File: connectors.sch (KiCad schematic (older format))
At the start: 4 parts

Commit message: finished schematic for review
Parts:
- removed J? (x3): Conn_01x06, symbol Connector_Generic:Conn_01x06
- added J? (x3): Conn_01x07, symbol Connector_Generic:Conn_01x07
- added J?: XLR5, symbol Connector:XLR5
- added R? (x15): 1K, symbol Device:R
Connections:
- net +12V: now also J?.1 (Pin_1), J?.1 (Pin_1), J?.1 (Pin_1)
- net Ch_1: now also J?.2 (Pin_2), R?.1
- net Ch_10: now also J?.6 (Pin_6), R?.1
- net Ch_11: now also J?.2 (Pin_2), R?.1
- net Ch_12: now also J?.3 (Pin_3), R?.1
- net Ch_2: now also J?.3 (Pin_3), R?.1
- net Ch_3: now also J?.4 (Pin_4), R?.1
- net Ch_4: now also J?.5 (Pin_5), R?.1
- net Ch_5: now also J?.6 (Pin_6), R?.1
- net Ch_6: now also J?.2 (Pin_2), R?.1
- net Ch_7: now also J?.3 (Pin_3), R?.1
- net Ch_8: now also J?.4 (Pin_4), R?.1
- net Ch_9: now also J?.5 (Pin_5), R?.1
- net GND: now also J?.4 (P3), J?.7 (Pin_7), J?.7 (Pin_7), J?.7 (Pin_7), R?.2, R?.2, R?.2, R?.2, R?.2, R?.2, R?.2, R?.2, R?.2, R?.2, R?.2, R?.2, R?.2, R?.2, R?.2
- net PPS: now also J?.3 (P3)
- net VCC: now also J?.5 (P5)
- net DI renamed RS485_A
- net RS485_A: now also J?.1 (P1)
- net RO renamed RS485_B
- net RS485_B: now also J?.2 (P2)
- new net Ch_13: J?.4 (Pin_4), R?.1
- new net Ch_14: J?.5 (Pin_5), R?.1
- new net Ch_15: J?.6 (Pin_6), R?.1

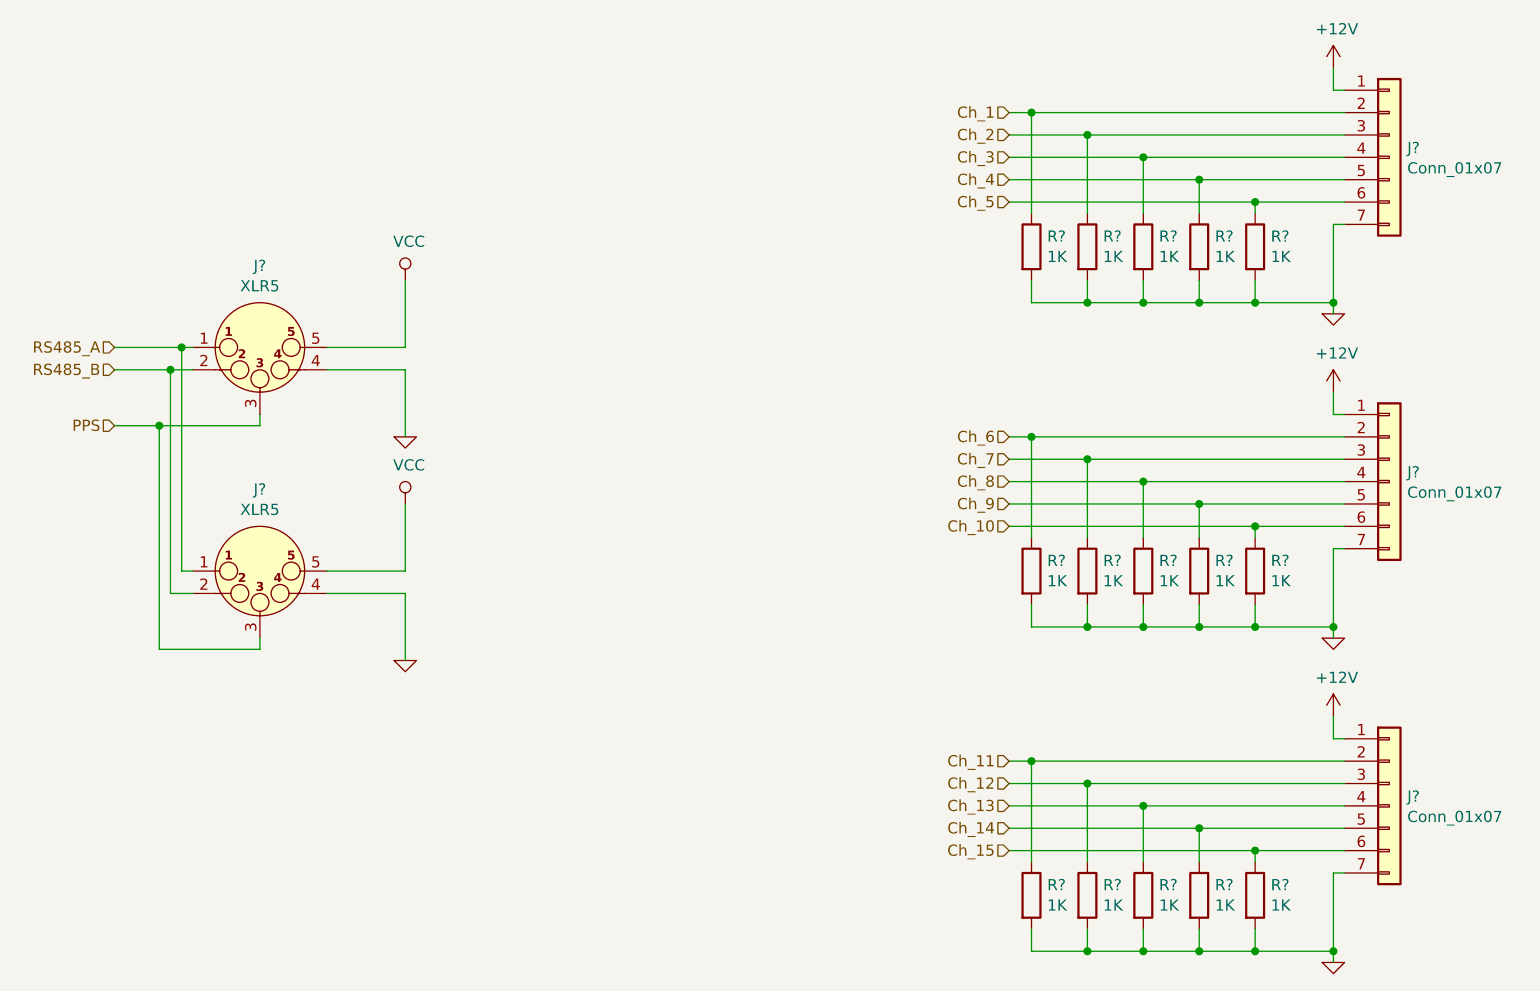
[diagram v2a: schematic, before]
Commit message: added pdf schematic
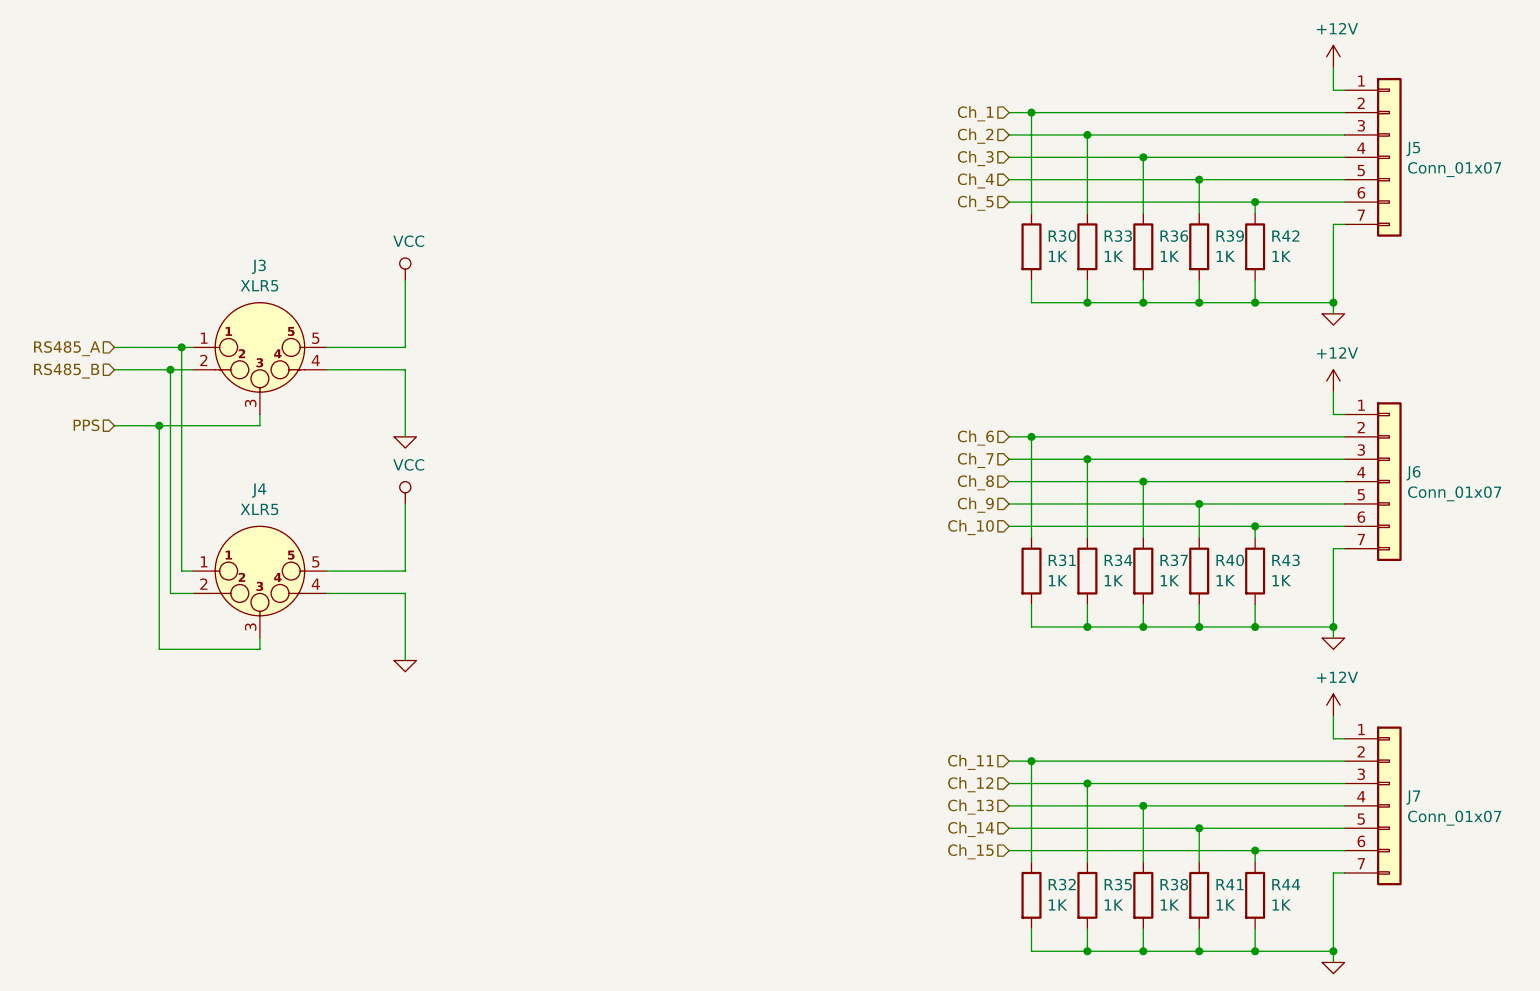
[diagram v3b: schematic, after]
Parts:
- gave numbers to parts that had none: 20
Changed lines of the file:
@@
 	8850 1750 8800 1750
 $Comp
-L daisy:GND #PWR?
+L daisy:GND #PWR052
 U 1 1 5D36F5B8
 P 8800 2150
-F 0 "#PWR?" H 8800 2150 30  0001 C CNN
+F 0 "#PWR052" H 8800 2150 30  0001 C CNN
 F 1 "GND" H 8800 2080 30  0001 C CNN
 F 2 "" H 8800 2150 60  0000 C CNN
@@
 	8800 1750 8800 2100
 $Comp
-L power:+12V #PWR?
+L power:+12V #PWR051
 U 1 1 5D36F5BF
 P 8800 1050
-F 0 "#PWR?" H 8800 900 50  0001 C CNN
+F 0 "#PWR051" H 8800 900 50  0001 C CNN
 F 1 "+12V" H 8815 1223 50  0000 C CNN
 F 2 "" H 8800 1050 50  0001 C CNN
@@
 Ch_4
 $Comp
-L Connector:XLR5 J?
+L Connector:XLR5 J3
 U 1 1 5D36FCC4
 P 4000 2300
-F 0 "J?" H 4000 2665 50  0000 C CNN
+F 0 "J3" H 4000 2665 50  0000 C CNN
 F 1 "XLR5" H 4000 2574 50  0000 C CNN
 F 2 "" H 4000 2300 50  0001 C CNN
@@
 	4300 2400 4650 2400
 $Comp
-L daisy:GND #PWR?
+L daisy:GND #PWR048
 U 1 1 5D37030E
 P 4650 2700
-F 0 "#PWR?" H 4650 2700 30  0001 C CNN
+F 0 "#PWR048" H 4650 2700 30  0001 C CNN
 F 1 "GND" H 4650 2630 30  0001 C CNN
 F 2 "" H 4650 2700 60  0000 C CNN
@@
 	4650 2400 4650 2700
 $Comp
-L power:VCC #PWR?
+L power:VCC #PWR047
 U 1 1 5D37054E
 P 4650 2000
-F 0 "#PWR?" H 4650 1850 50  0001 C CNN
+F 0 "#PWR047" H 4650 1850 50  0001 C CNN
 F 1 "VCC" H 4667 2173 50  0000 C CNN
 F 2 "" H 4650 2000 50  0001 C CNN
@@
 PPS
 $Comp
-L Connector_Generic:Conn_01x07 J?
+L Connector_Generic:Conn_01x07 J5
 U 1 1 5D5ED43F
 P 9050 1450
-F 0 "J?" H 9130 1492 50  0000 L CNN
+F 0 "J5" H 9130 1492 50  0000 L CNN
 F 1 "Conn_01x07" H 9130 1401 50  0000 L CNN
 F 2 "" H 9050 1450 50  0001 C CNN
@@
 Ch_5
 $Comp
-L Device:R R?
+L Device:R R42
 U 1 1 5D5EDE7E
 P 8450 1850
-F 0 "R?" H 8520 1896 50  0000 L CNN
+F 0 "R42" H 8520 1896 50  0000 L CNN
 F 1 "1K" H 8520 1805 50  0000 L CNN
 F 2 "" V 8380 1850 50  0001 C CNN
@@
 $EndComp
 $Comp
-L Device:R R?
+L Device:R R39
 U 1 1 5D5EE2E2
 P 8200 1850
-F 0 "R?" H 8270 1896 50  0000 L CNN
+F 0 "R39" H 8270 1896 50  0000 L CNN
 F 1 "1K" H 8270 1805 50  0000 L CNN
 F 2 "" V 8130 1850 50  0001 C CNN
@@
 $EndComp
 $Comp
-L Device:R R?
+L Device:R R36
 U 1 1 5D5EE304
 P 7950 1850
-F 0 "R?" H 8020 1896 50  0000 L CNN
+F 0 "R36" H 8020 1896 50  0000 L CNN
 F 1 "1K" H 8020 1805 50  0000 L CNN
 F 2 "" V 7880 1850 50  0001 C CNN
@@
 $EndComp
 $Comp
-L Device:R R?
+L Device:R R33
 U 1 1 5D5EE328
 P 7700 1850
-F 0 "R?" H 7770 1896 50  0000 L CNN
+F 0 "R33" H 7770 1896 50  0000 L CNN
 F 1 "1K" H 7770 1805 50  0000 L CNN
 F 2 "" V 7630 1850 50  0001 C CNN
@@
 $EndComp
 $Comp
-L Device:R R?
+L Device:R R30
 U 1 1 5D5EE34E
 P 7450 1850
-F 0 "R?" H 7520 1896 50  0000 L CNN
+F 0 "R30" H 7520 1896 50  0000 L CNN
 F 1 "1K" H 7520 1805 50  0000 L CNN
 F 2 "" V 7380 1850 50  0001 C CNN
@@
 	8850 3200 8800 3200
 $Comp
-L daisy:GND #PWR?
+L daisy:GND #PWR054
 U 1 1 5D5F47DC
 P 8800 3600
-F 0 "#PWR?" H 8800 3600 30  0001 C CNN
+F 0 "#PWR054" H 8800 3600 30  0001 C CNN
 F 1 "GND" H 8800 3530 30  0001 C CNN
 F 2 "" H 8800 3600 60  0000 C CNN
@@
 	8800 3200 8800 3550
 $Comp
-L power:+12V #PWR?
+L power:+12V #PWR053
 U 1 1 5D5F47E3
 P 8800 2500
-F 0 "#PWR?" H 8800 2350 50  0001 C CNN
+F 0 "#PWR053" H 8800 2350 50  0001 C CNN
 F 1 "+12V" H 8815 2673 50  0000 C CNN
 F 2 "" H 8800 2500 50  0001 C CNN
@@
 Ch_9
 $Comp
-L Connector_Generic:Conn_01x07 J?
+L Connector_Generic:Conn_01x07 J6
 U 1 1 5D5F47ED
 P 9050 2900
-F 0 "J?" H 9130 2942 50  0000 L CNN
+F 0 "J6" H 9130 2942 50  0000 L CNN
 F 1 "Conn_01x07" H 9130 2851 50  0000 L CNN
 F 2 "" H 9050 2900 50  0001 C CNN
@@
 Ch_10
 $Comp
-L Device:R R?
+L Device:R R43
 U 1 1 5D5F47F5
 P 8450 3300
-F 0 "R?" H 8520 3346 50  0000 L CNN
+F 0 "R43" H 8520 3346 50  0000 L CNN
 F 1 "1K" H 8520 3255 50  0000 L CNN
 F 2 "" V 8380 3300 50  0001 C CNN
@@
 $EndComp
 $Comp
-L Device:R R?
+L Device:R R40
 U 1 1 5D5F47FC
 P 8200 3300
-F 0 "R?" H 8270 3346 50  0000 L CNN
+F 0 "R40" H 8270 3346 50  0000 L CNN
 F 1 "1K" H 8270 3255 50  0000 L CNN
 F 2 "" V 8130 3300 50  0001 C CNN
@@
 $EndComp
 $Comp
-L Device:R R?
+L Device:R R37
 U 1 1 5D5F4803
 P 7950 3300
-F 0 "R?" H 8020 3346 50  0000 L CNN
+F 0 "R37" H 8020 3346 50  0000 L CNN
 F 1 "1K" H 8020 3255 50  0000 L CNN
 F 2 "" V 7880 3300 50  0001 C CNN
@@
 $EndComp
 $Comp
-L Device:R R?
+L Device:R R34
 U 1 1 5D5F480A
 P 7700 3300
-F 0 "R?" H 7770 3346 50  0000 L CNN
+F 0 "R34" H 7770 3346 50  0000 L CNN
 F 1 "1K" H 7770 3255 50  0000 L CNN
 F 2 "" V 7630 3300 50  0001 C CNN
@@
 $EndComp
 $Comp
-L Device:R R?
+L Device:R R31
 U 1 1 5D5F4811
 P 7450 3300
-F 0 "R?" H 7520 3346 50  0000 L CNN
+F 0 "R31" H 7520 3346 50  0000 L CNN
 F 1 "1K" H 7520 3255 50  0000 L CNN
 F 2 "" V 7380 3300 50  0001 C CNN
@@
 	8850 4650 8800 4650
 $Comp
-L daisy:GND #PWR?
+L daisy:GND #PWR056
 U 1 1 5D5F5C05
 P 8800 5050
-F 0 "#PWR?" H 8800 5050 30  0001 C CNN
+F 0 "#PWR056" H 8800 5050 30  0001 C CNN
 F 1 "GND" H 8800 4980 30  0001 C CNN
 F 2 "" H 8800 5050 60  0000 C CNN
@@
 	8800 4650 8800 5000
 $Comp
-L power:+12V #PWR?
+L power:+12V #PWR055
 U 1 1 5D5F5C0C
 P 8800 3950
-F 0 "#PWR?" H 8800 3800 50  0001 C CNN
+F 0 "#PWR055" H 8800 3800 50  0001 C CNN
 F 1 "+12V" H 8815 4123 50  0000 C CNN
 F 2 "" H 8800 3950 50  0001 C CNN
@@
 Ch_14
 $Comp
-L Connector_Generic:Conn_01x07 J?
+L Connector_Generic:Conn_01x07 J7
 U 1 1 5D5F5C16
 P 9050 4350
-F 0 "J?" H 9130 4392 50  0000 L CNN
+F 0 "J7" H 9130 4392 50  0000 L CNN
 F 1 "Conn_01x07" H 9130 4301 50  0000 L CNN
 F 2 "" H 9050 4350 50  0001 C CNN
@@
 Ch_15
 $Comp
-L Device:R R?
+L Device:R R44
 U 1 1 5D5F5C1E
 P 8450 4750
-F 0 "R?" H 8520 4796 50  0000 L CNN
+F 0 "R44" H 8520 4796 50  0000 L CNN
 F 1 "1K" H 8520 4705 50  0000 L CNN
 F 2 "" V 8380 4750 50  0001 C CNN
@@
 $EndComp
 $Comp
-L Device:R R?
+L Device:R R41
 U 1 1 5D5F5C25
 P 8200 4750
-F 0 "R?" H 8270 4796 50  0000 L CNN
+F 0 "R41" H 8270 4796 50  0000 L CNN
 F 1 "1K" H 8270 4705 50  0000 L CNN
 F 2 "" V 8130 4750 50  0001 C CNN
@@
 $EndComp
 $Comp
-L Device:R R?
+L Device:R R38
 U 1 1 5D5F5C2C
 P 7950 4750
-F 0 "R?" H 8020 4796 50  0000 L CNN
+F 0 "R38" H 8020 4796 50  0000 L CNN
 F 1 "1K" H 8020 4705 50  0000 L CNN
 F 2 "" V 7880 4750 50  0001 C CNN
@@
 $EndComp
 $Comp
-L Device:R R?
+L Device:R R35
 U 1 1 5D5F5C33
 P 7700 4750
-F 0 "R?" H 7770 4796 50  0000 L CNN
+F 0 "R35" H 7770 4796 50  0000 L CNN
 F 1 "1K" H 7770 4705 50  0000 L CNN
 F 2 "" V 7630 4750 50  0001 C CNN
@@
 $EndComp
 $Comp
-L Device:R R?
+L Device:R R32
 U 1 1 5D5F5C3A
 P 7450 4750
-F 0 "R?" H 7520 4796 50  0000 L CNN
+F 0 "R32" H 7520 4796 50  0000 L CNN
 F 1 "1K" H 7520 4705 50  0000 L CNN
 F 2 "" V 7380 4750 50  0001 C CNN
@@
 	8800 5000 8800 5050
 $Comp
-L Connector:XLR5 J?
+L Connector:XLR5 J4
 U 1 1 5D600577
 P 4000 3300
-F 0 "J?" H 4000 3665 50  0000 C CNN
+F 0 "J4" H 4000 3665 50  0000 C CNN
 F 1 "XLR5" H 4000 3574 50  0000 C CNN
 F 2 "" H 4000 3300 50  0001 C CNN
@@
 	4300 3400 4650 3400
 $Comp
-L daisy:GND #PWR?
+L daisy:GND #PWR050
 U 1 1 5D600585
 P 4650 3700
-F 0 "#PWR?" H 4650 3700 30  0001 C CNN
+F 0 "#PWR050" H 4650 3700 30  0001 C CNN
 F 1 "GND" H 4650 3630 30  0001 C CNN
 F 2 "" H 4650 3700 60  0000 C CNN
@@
 	4650 3400 4650 3700
 $Comp
-L power:VCC #PWR?
+L power:VCC #PWR049
 U 1 1 5D60058C
 P 4650 3000
-F 0 "#PWR?" H 4650 2850 50  0001 C CNN
+F 0 "#PWR049" H 4650 2850 50  0001 C CNN
 F 1 "VCC" H 4667 3173 50  0000 C CNN
 F 2 "" H 4650 3000 50  0001 C CNN

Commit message: started assigning footprints
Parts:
- J5, J6, J7: footprint (none) -> Connector_PinHeader_2.54mm:PinHeader_1x07_P2.54mm_Vertical
- R30, R31, R32, R33, R34, R35, R36, R37, R38, R39, R40, R41, R42, R43, R44: footprint (none) -> Resistor_SMD:R_0603_1608Metric
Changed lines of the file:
@@
 F 0 "J5" H 9130 1492 50  0000 L CNN
 F 1 "Conn_01x07" H 9130 1401 50  0000 L CNN
-F 2 "" H 9050 1450 50  0001 C CNN
+F 2 "Connector_PinHeader_2.54mm:PinHeader_1x07_P2.54mm_Vertical" H 9050 1450 50  0001 C CNN
 F 3 "~" H 9050 1450 50  0001 C CNN
 	1    9050 1450
@@
 F 0 "R42" H 8520 1896 50  0000 L CNN
 F 1 "1K" H 8520 1805 50  0000 L CNN
-F 2 "" V 8380 1850 50  0001 C CNN
+F 2 "Resistor_SMD:R_0603_1608Metric" V 8380 1850 50  0001 C CNN
 F 3 "~" H 8450 1850 50  0001 C CNN
 	1    8450 1850
@@
 F 0 "R39" H 8270 1896 50  0000 L CNN
 F 1 "1K" H 8270 1805 50  0000 L CNN
-F 2 "" V 8130 1850 50  0001 C CNN
+F 2 "Resistor_SMD:R_0603_1608Metric" V 8130 1850 50  0001 C CNN
 F 3 "~" H 8200 1850 50  0001 C CNN
 	1    8200 1850
@@
 F 0 "R36" H 8020 1896 50  0000 L CNN
 F 1 "1K" H 8020 1805 50  0000 L CNN
-F 2 "" V 7880 1850 50  0001 C CNN
+F 2 "Resistor_SMD:R_0603_1608Metric" V 7880 1850 50  0001 C CNN
 F 3 "~" H 7950 1850 50  0001 C CNN
 	1    7950 1850
@@
 F 0 "R33" H 7770 1896 50  0000 L CNN
 F 1 "1K" H 7770 1805 50  0000 L CNN
-F 2 "" V 7630 1850 50  0001 C CNN
+F 2 "Resistor_SMD:R_0603_1608Metric" V 7630 1850 50  0001 C CNN
 F 3 "~" H 7700 1850 50  0001 C CNN
 	1    7700 1850
@@
 F 0 "R30" H 7520 1896 50  0000 L CNN
 F 1 "1K" H 7520 1805 50  0000 L CNN
-F 2 "" V 7380 1850 50  0001 C CNN
+F 2 "Resistor_SMD:R_0603_1608Metric" V 7380 1850 50  0001 C CNN
 F 3 "~" H 7450 1850 50  0001 C CNN
 	1    7450 1850
@@
 F 0 "J6" H 9130 2942 50  0000 L CNN
 F 1 "Conn_01x07" H 9130 2851 50  0000 L CNN
-F 2 "" H 9050 2900 50  0001 C CNN
+F 2 "Connector_PinHeader_2.54mm:PinHeader_1x07_P2.54mm_Vertical" H 9050 2900 50  0001 C CNN
 F 3 "~" H 9050 2900 50  0001 C CNN
 	1    9050 2900
@@
 F 0 "R43" H 8520 3346 50  0000 L CNN
 F 1 "1K" H 8520 3255 50  0000 L CNN
-F 2 "" V 8380 3300 50  0001 C CNN
+F 2 "Resistor_SMD:R_0603_1608Metric" V 8380 3300 50  0001 C CNN
 F 3 "~" H 8450 3300 50  0001 C CNN
 	1    8450 3300
@@
 F 0 "R40" H 8270 3346 50  0000 L CNN
 F 1 "1K" H 8270 3255 50  0000 L CNN
-F 2 "" V 8130 3300 50  0001 C CNN
+F 2 "Resistor_SMD:R_0603_1608Metric" V 8130 3300 50  0001 C CNN
 F 3 "~" H 8200 3300 50  0001 C CNN
 	1    8200 3300
@@
 F 0 "R37" H 8020 3346 50  0000 L CNN
 F 1 "1K" H 8020 3255 50  0000 L CNN
-F 2 "" V 7880 3300 50  0001 C CNN
+F 2 "Resistor_SMD:R_0603_1608Metric" V 7880 3300 50  0001 C CNN
 F 3 "~" H 7950 3300 50  0001 C CNN
 	1    7950 3300
@@
 F 0 "R34" H 7770 3346 50  0000 L CNN
 F 1 "1K" H 7770 3255 50  0000 L CNN
-F 2 "" V 7630 3300 50  0001 C CNN
+F 2 "Resistor_SMD:R_0603_1608Metric" V 7630 3300 50  0001 C CNN
 F 3 "~" H 7700 3300 50  0001 C CNN
 	1    7700 3300
@@
 F 0 "R31" H 7520 3346 50  0000 L CNN
 F 1 "1K" H 7520 3255 50  0000 L CNN
-F 2 "" V 7380 3300 50  0001 C CNN
+F 2 "Resistor_SMD:R_0603_1608Metric" V 7380 3300 50  0001 C CNN
 F 3 "~" H 7450 3300 50  0001 C CNN
 	1    7450 3300
@@
 F 0 "J7" H 9130 4392 50  0000 L CNN
 F 1 "Conn_01x07" H 9130 4301 50  0000 L CNN
-F 2 "" H 9050 4350 50  0001 C CNN
+F 2 "Connector_PinHeader_2.54mm:PinHeader_1x07_P2.54mm_Vertical" H 9050 4350 50  0001 C CNN
 F 3 "~" H 9050 4350 50  0001 C CNN
 	1    9050 4350
@@
 F 0 "R44" H 8520 4796 50  0000 L CNN
 F 1 "1K" H 8520 4705 50  0000 L CNN
-F 2 "" V 8380 4750 50  0001 C CNN
+F 2 "Resistor_SMD:R_0603_1608Metric" V 8380 4750 50  0001 C CNN
 F 3 "~" H 8450 4750 50  0001 C CNN
 	1    8450 4750
@@
 F 0 "R41" H 8270 4796 50  0000 L CNN
 F 1 "1K" H 8270 4705 50  0000 L CNN
-F 2 "" V 8130 4750 50  0001 C CNN
+F 2 "Resistor_SMD:R_0603_1608Metric" V 8130 4750 50  0001 C CNN
 F 3 "~" H 8200 4750 50  0001 C CNN
 	1    8200 4750
@@
 F 0 "R38" H 8020 4796 50  0000 L CNN
 F 1 "1K" H 8020 4705 50  0000 L CNN
-F 2 "" V 7880 4750 50  0001 C CNN
+F 2 "Resistor_SMD:R_0603_1608Metric" V 7880 4750 50  0001 C CNN
 F 3 "~" H 7950 4750 50  0001 C CNN
 	1    7950 4750
@@
 F 0 "R35" H 7770 4796 50  0000 L CNN
 F 1 "1K" H 7770 4705 50  0000 L CNN
-F 2 "" V 7630 4750 50  0001 C CNN
+F 2 "Resistor_SMD:R_0603_1608Metric" V 7630 4750 50  0001 C CNN
 F 3 "~" H 7700 4750 50  0001 C CNN
 	1    7700 4750
@@
 F 0 "R32" H 7520 4796 50  0000 L CNN
 F 1 "1K" H 7520 4705 50  0000 L CNN
-F 2 "" V 7380 4750 50  0001 C CNN
+F 2 "Resistor_SMD:R_0603_1608Metric" V 7380 4750 50  0001 C CNN
 F 3 "~" H 7450 4750 50  0001 C CNN
 	1    7450 4750
